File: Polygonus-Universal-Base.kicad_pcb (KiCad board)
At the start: 2 copper layers, 160 x 118 mm, 78 parts, among them J1 Conn_02x04_Top_Bottom, J4 Polygonus_Plugs, J5 Conn_02x04_Top_Bottom, Q1 NGD8201AN, Q2 NGD8201AN, Q3 NGD8201AN, Q4 NGD8201AN, Q5 NGD8201AN, Q6 NGD8201AN, Q7 NGD8201AN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

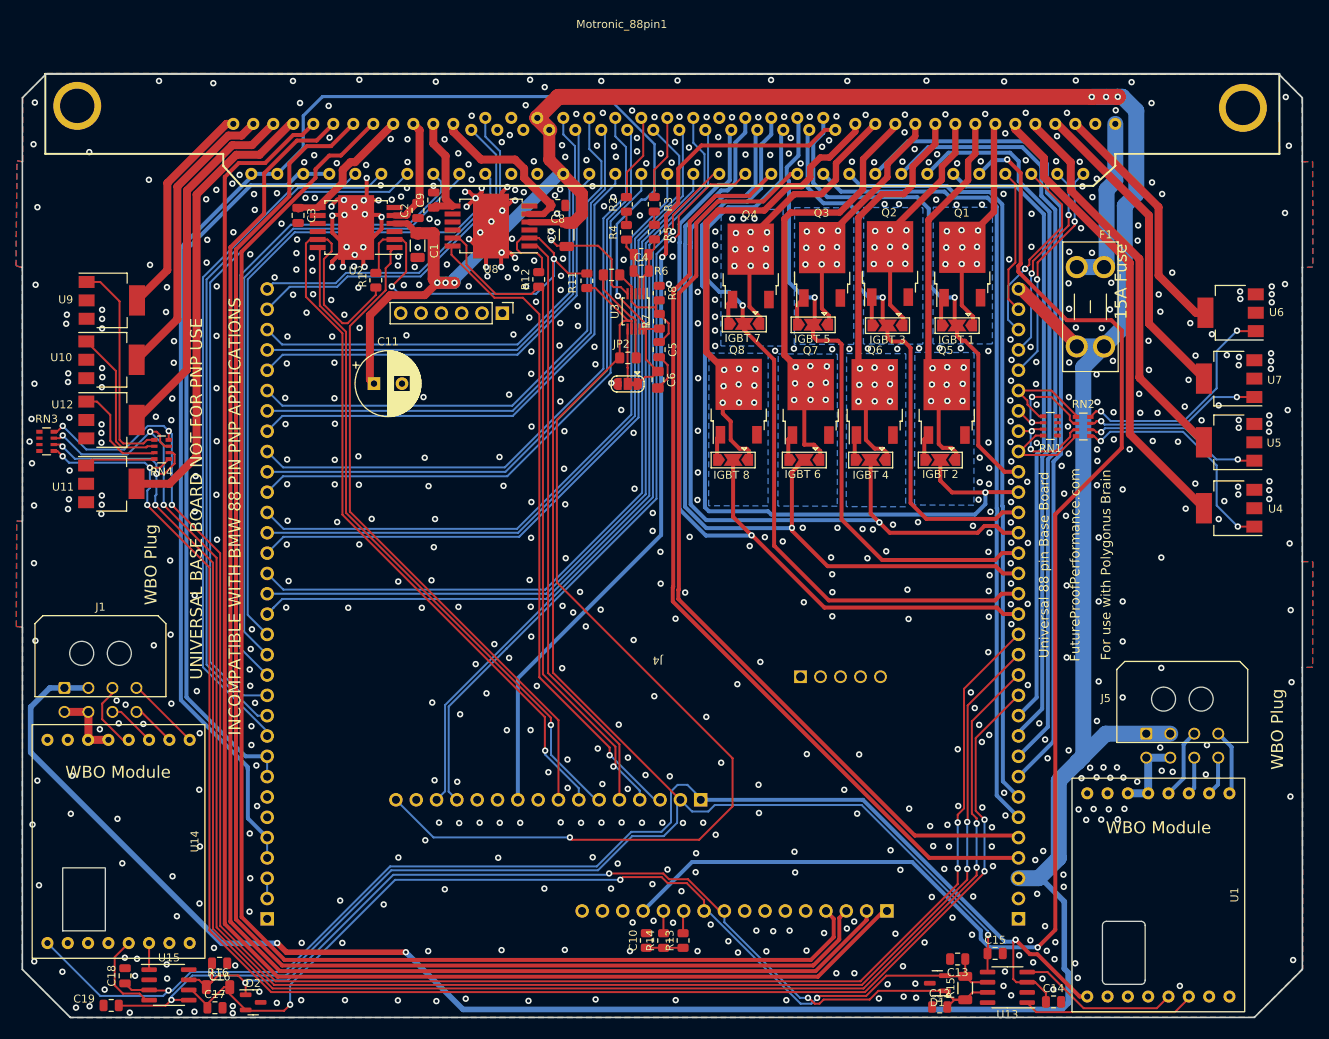
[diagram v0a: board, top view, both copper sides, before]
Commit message: silkscreen/erc tweaks
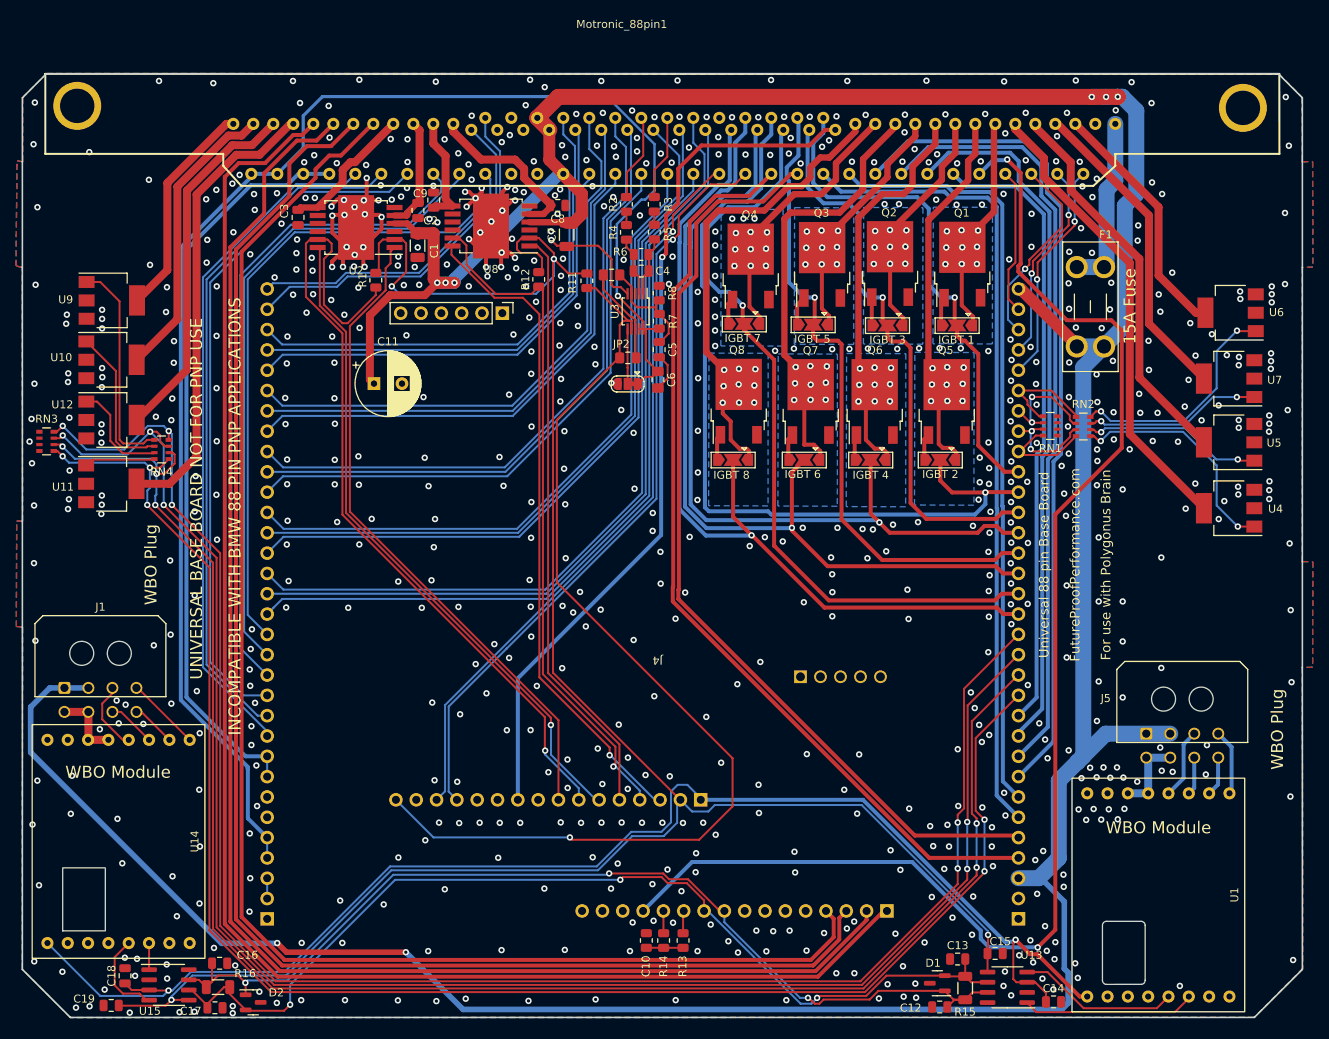
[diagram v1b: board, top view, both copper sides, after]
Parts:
- moved C3 0.26 mm to (91.6, 44.3)
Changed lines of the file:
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@@
     (property "ki_keywords" "High-Speed CAN Transceiver")
     (attr smd)
-    (fp_text reference "U15" (at 0 -3.4) (layer "F.SilkS")
+    (fp_text reference "U15" (at -2.381624 3.268455) (layer "F.SilkS")
         (effects (font (size 1 1) (thickness 0.15)))
     )
@@
     (property "ki_keywords" "cap capacitor")
     (attr smd)
-    (fp_text reference "C15" (at 0 -1.68) (layer "F.SilkS")
+    (fp_text reference "C15" (at 0.644474 -1.5) (layer "F.SilkS")
         (effects (font (size 1 1) (thickness 0.15)))
     )
@@
     (property "ki_keywords" "cap capacitor")
     (attr smd)
-    (fp_text reference "C16" (at 0 -1.68) (layer "F.SilkS")
+    (fp_text reference "C16" (at -3.481833 1.023839) (layer "F.SilkS")
         (effects (font (size 1 1) (thickness 0.15)))
     )
@@
     (property "ki_keywords" "cap capacitor")
     (attr smd)
-    (fp_text reference "C13" (at 0 -1.68) (layer "F.SilkS")
+    (fp_text reference "C13" (at 0 1.698591) (layer "F.SilkS")
         (effects (font (size 1 1) (thickness 0.15)))
     )
@@
     (property "ki_keywords" "cap capacitor")
     (attr smd)
-    (fp_text reference "C17" (at 0 -1.68) (layer "F.SilkS")
+    (fp_text reference "C17" (at -3.034731 0.408171) (layer "F.SilkS")
         (effects (font (size 1 1) (thickness 0.15)))
     )
@@
     (property "ki_keywords" "cap capacitor")
     (attr smd)
-    (fp_text reference "C12" (at 0 -1.68) (layer "F.SilkS")
+    (fp_text reference "C12" (at -3.627796 0.108955) (layer "F.SilkS")
         (effects (font (size 1 1) (thickness 0.15)))
     )
@@
     (property "ki_keywords" "R res resistor")
     (attr smd)
-    (fp_text reference "R6" (at -2.489589 -2.072209) (layer "F.SilkS")
+    (fp_text reference "R6" (at 2.609372 0.324572) (layer "F.SilkS")
         (effects (font (size 1 1) (thickness 0.15)))
     )
@@
     (property "ki_keywords" "R res resistor")
     (attr smd exclude_from_bom)
-    (fp_text reference "R15" (at 0 -1.82 90) (layer "F.SilkS")
+    (fp_text reference "R15" (at -2.97387 -0.014418 180) (layer "F.SilkS")
         (effects (font (size 1 1) (thickness 0.15)))
     )
@@
     (property "ki_description" "Resistor")
     (attr smd)
-    (fp_text reference "R14" (at 0 -1.65 90) (layer "F.SilkS")
+    (fp_text reference "R14" (at -3.21588 -0.016345 90) (layer "F.SilkS")
         (effects (font (size 1 1) (thickness 0.15)))
     )
@@
     (property "ki_keywords" "R res resistor")
     (attr smd exclude_from_bom)
-    (fp_text reference "R16" (at 0 -1.82) (layer "F.SilkS")
+    (fp_text reference "R16" (at 3.38225 -1.710045) (layer "F.SilkS")
         (effects (font (size 1 1) (thickness 0.15)))
     )
@@
     (property "ki_keywords" "can esd protection suppression transient")
     (attr smd)
-    (fp_text reference "D1" (at 0 -2.4) (layer "F.SilkS")
+    (fp_text reference "D1" (at 0.527171 2.52488) (layer "F.SilkS")
         (effects (font (size 1 1) (thickness 0.15)))
     )
@@
     (property "ki_keywords" "R res resistor")
     (attr smd)
-    (fp_text reference "R7" (at 0 -1.65 90) (layer "F.SilkS")
+    (fp_text reference "R7" (at 0 1.722843 90) (layer "F.SilkS")
         (effects (font (size 1 1) (thickness 0.15)))
     )
@@
   )
   (footprint "Capacitor_SMD:C_0805_2012Metric" (layer "F.Cu")
-    (at 91.623348 44.083893 -90)
+    (at 91.623348 44.34 -90)
     (descr "Capacitor SMD 0805 (2012 Metric), square (rectangular) end terminal, IPC_7351 nominal, (Body size source: IPC-SM-782 page 76, https://www.pcb-3d.com/wordpress/wp-content/uploads/ipc-sm-782a_amendment_1_and_2.pdf, https://docs.google.com/spreadsheets/d/1BsfQQcO9C6DZCsRaXUlFlo91Tg2WpOkGARC1WS5S8t0/edit?usp=sharing), generated with kicad-footprint-generator")
     (tags "capacitor")
@@
     (property "ki_keywords" "capacitor cap")
     (attr smd)
-    (fp_text reference "C3" (at 0 -1.68 -90) (layer "F.SilkS")
+    (fp_text reference "C3" (at -0.8 1.723348 -90) (layer "F.SilkS")
         (effects (font (size 1 1) (thickness 0.15)))
     )
@@
     (property "ki_keywords" "can esd protection suppression transient")
     (attr smd)
-    (fp_text reference "D2" (at 0 -2.4) (layer "F.SilkS")
+    (fp_text reference "D2" (at 2.893128 -1.214002) (layer "F.SilkS")
         (effects (font (size 1 1) (thickness 0.15)))
     )
@@
     (property "ki_keywords" "High-Speed CAN Transceiver")
     (attr smd)
-    (fp_text reference "U13" (at 0 -3.4) (layer "F.SilkS")
+    (fp_text reference "U13" (at -3.014407 4.033446) (layer "F.SilkS")
         (effects (font (size 1 1) (thickness 0.15)))
     )
@@
     (property "ki_description" "Resistor")
     (attr smd)
-    (fp_text reference "R13" (at 0 -1.65 90) (layer "F.SilkS")
+    (fp_text reference "R13" (at -3.21588 -0.04911 90) (layer "F.SilkS")
         (effects (font (size 1 1) (thickness 0.15)))
     )
@@
     (property "ki_keywords" "capacitor cap")
     (attr smd)
-    (fp_text reference "C9" (at 0 -1.68 90) (layer "F.SilkS")
+    (fp_text reference "C9" (at 0.828935 -1.679658 180) (layer "F.SilkS")
         (effects (font (size 1 1) (thickness 0.15)))
     )
@@
     (property "ki_description" "Resistor")
     (attr smd)
-    (fp_text reference "C10" (at 0 -1.65 90) (layer "F.SilkS")
+    (fp_text reference "C10" (at -3.223867 -0.057194 90) (layer "F.SilkS")
         (effects (font (size 1 1) (thickness 0.15)))
     )
@@
     (property "ki_keywords" "cap capacitor")
     (attr smd)
-    (fp_text reference "C4" (at 0 -1.68) (layer "F.SilkS")
+    (fp_text reference "C4" (at 2.690628 -0.001904) (layer "F.SilkS")
         (effects (font (size 1 1) (thickness 0.15)))
     )
@@
     (property "ki_keywords" "capacitor cap")
     (attr smd)
-    (fp_text reference "C2" (at 0 -1.68 90) (layer "F.SilkS")
+    (fp_text reference "C2" (at -1.273532 1.587405 180) (layer "F.SilkS")
         (effects (font (size 1 1) (thickness 0.15)))
     )
@@
     (effects (font (size 1 1) (thickness 0.15)))
   )
-  (gr_text "15A Fuse" (at 194.48984 52.361877 90) (layer "F.SilkS")
+  (gr_text "15A Fuse" (at 195.6 55.44 90) (layer "F.SilkS")
     (effects (font (size 1.5 1.5) (thickness 0.3)))
   )
@@
   (via (at 152.974191 36.3535) (size 0.8) (drill 0.4) (layers "F.Cu" "B.Cu") (free) (net 2))
   (via (at 131.709666 107.736671) (size 0.8) (drill 0.4) (layers "F.Cu" "B.Cu") (free) (net 2))
-  (via (at 123.982479 43.859855) (size 0.8) (drill 0.4) (layers "F.Cu" "B.Cu") (free) (net 2))
+  (via (at 124.051879 43.90397) (size 0.8) (drill 0.4) (layers "F.Cu" "B.Cu") (free) (net 2))
   (via (at 76.114639 59.801059) (size 0.8) (drill 0.4) (layers "F.Cu" "B.Cu") (free) (net 2))
   (via (at 177.984966 77.644702) (size 0.8) (drill 0.4) (layers "F.Cu" "B.Cu") (free) (net 2))
@@
   (segment (start 98.739011 37.431005) (end 98.172121 37.431005) (width 1) (layer "F.Cu") (net 107))
   (segment (start 98.172121 37.431005) (end 97.197372 38.405754) (width 1) (layer "F.Cu") (net 107))
-  (segment (start 91.670481 43.308893) (end 91.623348 43.308893) (width 0.8) (layer "F.Cu") (net 107))
-  (segment (start 94.077537 43.096167) (end 91.883207 43.096167) (width 0.8) (layer "F.Cu") (net 107))
+  (segment (start 91.917181 43.096167) (end 94.077537 43.096167) (width 0.8) (layer "F.Cu") (net 107))
   (segment (start 97.197372 38.405754) (end 97.197372 39.976332) (width 1) (layer "F.Cu") (net 107))
-  (segment (start 91.883207 43.096167) (end 91.670481 43.308893) (width 0.8) (layer "F.Cu") (net 107))
+  (segment (start 91.623348 43.39) (end 91.917181 43.096167) (width 0.8) (layer "F.Cu") (net 107))
   (segment (start 97.197372 39.976332) (end 94.077537 43.096167) (width 0.9) (layer "F.Cu") (net 107))
   (segment (start 114.510015 37.101985) (end 118.736425 37.101985) (width 1) (layer "F.Cu") (net 108))

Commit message: fix wideband library, ERC, DRC
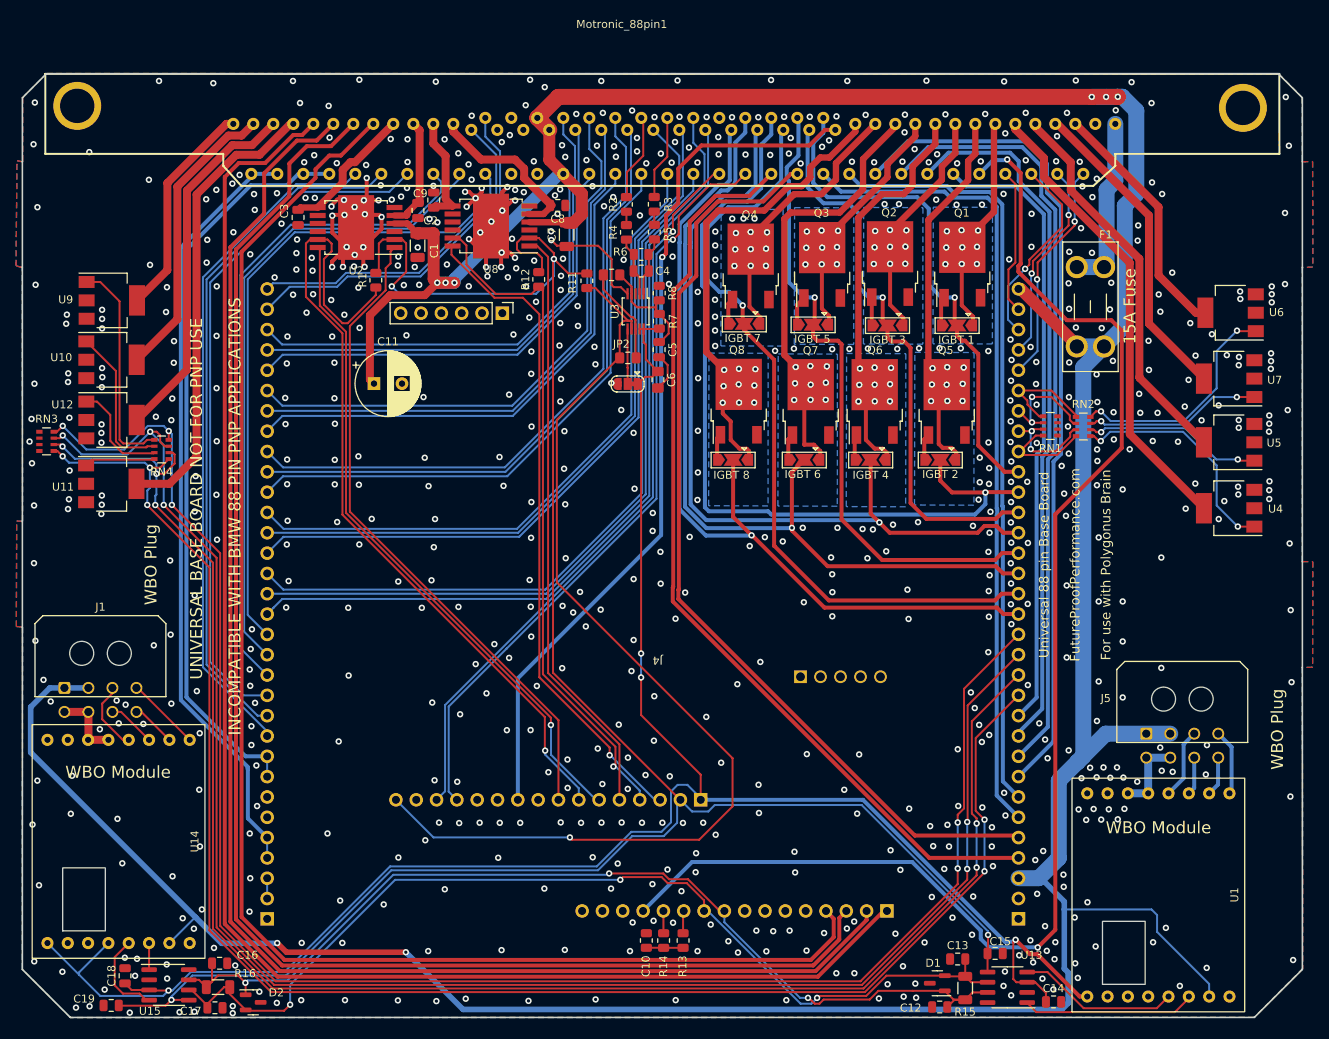
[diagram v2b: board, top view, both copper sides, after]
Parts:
- U1: value WBO-Single-Module -> f042_wideband_module; footprint Simon:f042_wideband_module -> wideband_module:f042_wideband_module
- U14: value WBO-Single-Module -> f042_wideband_module
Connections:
- net /+3V3 renamed +3.3V
- C14 pad 1: /+5V -> +5V
- C18 pad 1: /+5V -> +5V
- C6 pad 1: /5V_SENSOR_2 -> +5V
- J4 pad 81: /+5V -> +5V
- JP2 pad 1: /5V_SENSOR_2 -> +5V
- R7 pad 1: /5V_SENSOR_2 -> +5V
- U1 pad 1: /+5V -> +5V
- U1 pad 7: unconnected-(U1-Pad7) -> /12V_MR_FUSE
- U13 pad 3: /+5V -> +5V
- U14 pad 1: /+5V -> +5V
- U14 pad 3: GND -> unconnected-(U14-SEL_1-Pad3)
- U14 pad 4: unconnected-(U14-Select2-Pad4) -> +5V
- U14 pad 7: unconnected-(U14-nRESET-Pad7) -> /12V_MR_FUSE
- U15 pad 3: /+5V -> +5V
- U3 pad 10: /5V_SENSOR_2 -> +5V
- U3 pad 9: /5V_SENSOR_2 -> +5V
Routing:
- net +5V: track 0.00 -> 246.3 mm, vias 0 -> 4
- net /+5V: track 173.9 -> 0.00 mm, vias 2 -> 0
- net /5V_SENSOR_2: track 191.0 -> 96.9 mm, vias 1 -> 0
- net /12V_MR_FUSE: track 463.2 -> 492.6 mm
- net GND: vias 726 -> 741
